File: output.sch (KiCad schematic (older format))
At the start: 14 parts

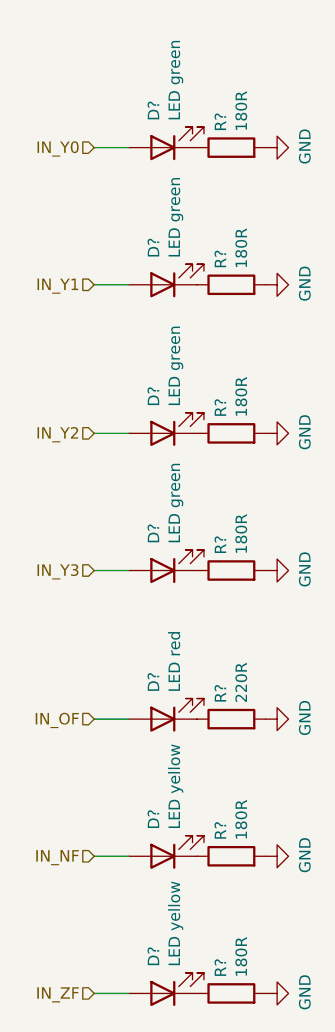
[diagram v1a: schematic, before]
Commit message: Annotate components in input and output
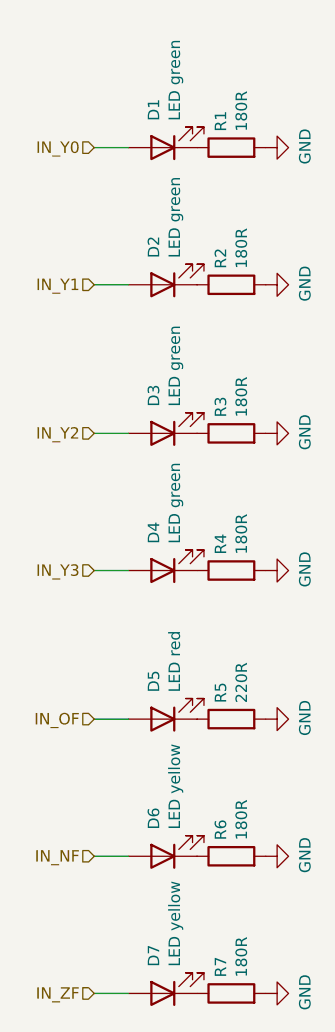
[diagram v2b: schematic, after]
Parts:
- gave numbers to parts that had none: 14
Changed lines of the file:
@@
 P 2050 1600
 AR Path="/604E77BF" Ref="D?"  Part="1"
-AR Path="/60318070/604E77BF" Ref="D?"  Part="1"
-F 0 "D?" V 2089 1483 50  0000 R CNN
+AR Path="/60318070/604E77BF" Ref="D2"  Part="1"
+F 0 "D2" V 2089 1483 50  0000 R CNN
 F 1 "LED green" V 1998 1483 50  0000 R CNN
 F 2 "LEDs:LED_0603" H 2050 1600 50  0001 C CNN
@@
 P 2350 1600
 AR Path="/604E77C6" Ref="R?"  Part="1"
-AR Path="/60318070/604E77C6" Ref="R?"  Part="1"
-F 0 "R?" H 2420 1646 50  0000 L CNN
+AR Path="/60318070/604E77C6" Ref="R2"  Part="1"
+F 0 "R2" H 2420 1646 50  0000 L CNN
 F 1 "180R" H 2420 1555 50  0000 L CNN
 F 2 "Resistors_SMD:R_0603" V 2280 1600 50  0001 C CNN
@@
 P 2050 2250
 AR Path="/604E84F3" Ref="D?"  Part="1"
-AR Path="/60318070/604E84F3" Ref="D?"  Part="1"
-F 0 "D?" V 2089 2133 50  0000 R CNN
+AR Path="/60318070/604E84F3" Ref="D3"  Part="1"
+F 0 "D3" V 2089 2133 50  0000 R CNN
 F 1 "LED green" V 1998 2133 50  0000 R CNN
 F 2 "LEDs:LED_0603" H 2050 2250 50  0001 C CNN
@@
 P 2350 2250
 AR Path="/604E84FA" Ref="R?"  Part="1"
-AR Path="/60318070/604E84FA" Ref="R?"  Part="1"
-F 0 "R?" H 2420 2296 50  0000 L CNN
+AR Path="/60318070/604E84FA" Ref="R3"  Part="1"
+F 0 "R3" H 2420 2296 50  0000 L CNN
 F 1 "180R" H 2420 2205 50  0000 L CNN
 F 2 "Resistors_SMD:R_0603" V 2280 2250 50  0001 C CNN
@@
 P 2050 2850
 AR Path="/604E912A" Ref="D?"  Part="1"
-AR Path="/60318070/604E912A" Ref="D?"  Part="1"
-F 0 "D?" V 2089 2733 50  0000 R CNN
+AR Path="/60318070/604E912A" Ref="D4"  Part="1"
+F 0 "D4" V 2089 2733 50  0000 R CNN
 F 1 "LED green" V 1998 2733 50  0000 R CNN
 F 2 "LEDs:LED_0603" H 2050 2850 50  0001 C CNN
@@
 P 2350 2850
 AR Path="/604E9131" Ref="R?"  Part="1"
-AR Path="/60318070/604E9131" Ref="R?"  Part="1"
-F 0 "R?" H 2420 2896 50  0000 L CNN
+AR Path="/60318070/604E9131" Ref="R4"  Part="1"
+F 0 "R4" H 2420 2896 50  0000 L CNN
 F 1 "180R" H 2420 2805 50  0000 L CNN
 F 2 "Resistors_SMD:R_0603" V 2280 2850 50  0001 C CNN
@@
 P 2350 3500
 AR Path="/60506BF5" Ref="R?"  Part="1"
-AR Path="/60318070/60506BF5" Ref="R?"  Part="1"
-F 0 "R?" H 2420 3546 50  0000 L CNN
+AR Path="/60318070/60506BF5" Ref="R5"  Part="1"
+F 0 "R5" H 2420 3546 50  0000 L CNN
 F 1 "220R" H 2420 3455 50  0000 L CNN
 F 2 "Resistors_SMD:R_0603" V 2280 3500 50  0001 C CNN
@@
 P 2050 3500
 AR Path="/60506BFC" Ref="D?"  Part="1"
-AR Path="/60318070/60506BFC" Ref="D?"  Part="1"
-F 0 "D?" V 2089 3383 50  0000 R CNN
+AR Path="/60318070/60506BFC" Ref="D5"  Part="1"
+F 0 "D5" V 2089 3383 50  0000 R CNN
 F 1 "LED red" V 1998 3383 50  0000 R CNN
 F 2 "LEDs:LED_0603" H 2050 3500 50  0001 C CNN
@@
 	1750 3500 1900 3500
 $Comp
-L Device:LED D?
+L Device:LED D6
 U 1 1 6052228B
 P 2050 4100
-F 0 "D?" V 2089 3983 50  0000 R CNN
+F 0 "D6" V 2089 3983 50  0000 R CNN
 F 1 "LED yellow" V 1998 3983 50  0000 R CNN
 F 2 "LEDs:LED_0603" H 2050 4100 50  0001 C CNN
@@
 $EndComp
 $Comp
-L Device:R R?
+L Device:R R6
 U 1 1 60522292
 P 2350 4100
-F 0 "R?" H 2420 4146 50  0000 L CNN
+F 0 "R6" H 2420 4146 50  0000 L CNN
 F 1 "180R" H 2420 4055 50  0000 L CNN
 F 2 "Resistors_SMD:R_0603" V 2280 4100 50  0001 C CNN
@@
 $EndComp
 $Comp
-L Device:LED D?
+L Device:LED D7
 U 1 1 60522C47
 P 2050 4700
-F 0 "D?" V 2089 4583 50  0000 R CNN
+F 0 "D7" V 2089 4583 50  0000 R CNN
 F 1 "LED yellow" V 1998 4583 50  0000 R CNN
 F 2 "LEDs:LED_0603" H 2050 4700 50  0001 C CNN
@@
 $EndComp
 $Comp
-L Device:R R?
+L Device:R R7
 U 1 1 60522C4E
 P 2350 4700
-F 0 "R?" H 2420 4746 50  0000 L CNN
+F 0 "R7" H 2420 4746 50  0000 L CNN
 F 1 "180R" H 2420 4655 50  0000 L CNN
 F 2 "Resistors_SMD:R_0603" V 2280 4700 50  0001 C CNN
@@
 P 2350 1000
 AR Path="/604E723F" Ref="R?"  Part="1"
-AR Path="/60318070/604E723F" Ref="R?"  Part="1"
-F 0 "R?" H 2420 1046 50  0000 L CNN
+AR Path="/60318070/604E723F" Ref="R1"  Part="1"
+F 0 "R1" H 2420 1046 50  0000 L CNN
 F 1 "180R" H 2420 955 50  0000 L CNN
 F 2 "Resistors_SMD:R_0603" V 2280 1000 50  0001 C CNN
@@
 P 2050 1000
 AR Path="/604E7238" Ref="D?"  Part="1"
-AR Path="/60318070/604E7238" Ref="D?"  Part="1"
-F 0 "D?" V 2089 883 50  0000 R CNN
+AR Path="/60318070/604E7238" Ref="D1"  Part="1"
+F 0 "D1" V 2089 883 50  0000 R CNN
 F 1 "LED green" V 1998 883 50  0000 R CNN
 F 2 "LEDs:LED_0603" H 2050 1000 50  0001 C CNN

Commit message: fixed some footprints
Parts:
- D1: footprint LEDs:LED_0603 -> LED_SMD:LED_0603_1608Metric
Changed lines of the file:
@@
 F 0 "D1" V 2089 883 50  0000 R CNN
 F 1 "LED green" V 1998 883 50  0000 R CNN
-F 2 "LEDs:LED_0603" H 2050 1000 50  0001 C CNN
+F 2 "LED_SMD:LED_0603_1608Metric" H 2050 1000 50  0001 C CNN
 F 3 "https://datasheet.lcsc.com/szlcsc/1811101510_Everlight-Elec-19-217-GHC-YR1S2-3T_C72043.pdf" H 2050 1000 50  0001 C CNN
 F 4 "C72043" V 2050 1000 50  0001 C CNN "LCSC"

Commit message: Change R, C and LED footprints
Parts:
- D2, D3, D4, D5, D6, D7: footprint LEDs:LED_0603 -> LED_SMD:LED_0603_1608Metric
- R1, R2, R3, R4, R5, R6, R7: footprint Resistors_SMD:R_0603 -> Resistor_SMD:R_0603_1608Metric
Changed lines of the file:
@@
 F 0 "D2" V 2089 1483 50  0000 R CNN
 F 1 "LED green" V 1998 1483 50  0000 R CNN
-F 2 "LEDs:LED_0603" H 2050 1600 50  0001 C CNN
+F 2 "LED_SMD:LED_0603_1608Metric" H 2050 1600 50  0001 C CNN
 F 3 "https://datasheet.lcsc.com/szlcsc/1811101510_Everlight-Elec-19-217-GHC-YR1S2-3T_C72043.pdf" H 2050 1600 50  0001 C CNN
 F 4 "C72043" V 2050 1600 50  0001 C CNN "LCSC"
@@
 F 0 "R2" H 2420 1646 50  0000 L CNN
 F 1 "180R" H 2420 1555 50  0000 L CNN
-F 2 "Resistors_SMD:R_0603" V 2280 1600 50  0001 C CNN
+F 2 "Resistor_SMD:R_0603_1608Metric" V 2280 1600 50  0001 C CNN
 F 3 "https://datasheet.lcsc.com/szlcsc/Uniroyal-Elec-0603WAF1800T5E_C22828.pdf" H 2350 1600 50  0001 C CNN
 F 4 "C22828" H 2350 1600 50  0001 C CNN "LCSC"
@@
 F 0 "D3" V 2089 2133 50  0000 R CNN
 F 1 "LED green" V 1998 2133 50  0000 R CNN
-F 2 "LEDs:LED_0603" H 2050 2250 50  0001 C CNN
+F 2 "LED_SMD:LED_0603_1608Metric" H 2050 2250 50  0001 C CNN
 F 3 "https://datasheet.lcsc.com/szlcsc/1811101510_Everlight-Elec-19-217-GHC-YR1S2-3T_C72043.pdf" H 2050 2250 50  0001 C CNN
 F 4 "C72043" V 2050 2250 50  0001 C CNN "LCSC"
@@
 F 0 "R3" H 2420 2296 50  0000 L CNN
 F 1 "180R" H 2420 2205 50  0000 L CNN
-F 2 "Resistors_SMD:R_0603" V 2280 2250 50  0001 C CNN
+F 2 "Resistor_SMD:R_0603_1608Metric" V 2280 2250 50  0001 C CNN
 F 3 "https://datasheet.lcsc.com/szlcsc/Uniroyal-Elec-0603WAF1800T5E_C22828.pdf" H 2350 2250 50  0001 C CNN
 F 4 "C22828" H 2350 2250 50  0001 C CNN "LCSC"
@@
 F 0 "D4" V 2089 2733 50  0000 R CNN
 F 1 "LED green" V 1998 2733 50  0000 R CNN
-F 2 "LEDs:LED_0603" H 2050 2850 50  0001 C CNN
+F 2 "LED_SMD:LED_0603_1608Metric" H 2050 2850 50  0001 C CNN
 F 3 "https://datasheet.lcsc.com/szlcsc/1811101510_Everlight-Elec-19-217-GHC-YR1S2-3T_C72043.pdf" H 2050 2850 50  0001 C CNN
 F 4 "C72043" V 2050 2850 50  0001 C CNN "LCSC"
@@
 F 0 "R4" H 2420 2896 50  0000 L CNN
 F 1 "180R" H 2420 2805 50  0000 L CNN
-F 2 "Resistors_SMD:R_0603" V 2280 2850 50  0001 C CNN
+F 2 "Resistor_SMD:R_0603_1608Metric" V 2280 2850 50  0001 C CNN
 F 3 "https://datasheet.lcsc.com/szlcsc/Uniroyal-Elec-0603WAF1800T5E_C22828.pdf" H 2350 2850 50  0001 C CNN
 F 4 "C22828" H 2350 2850 50  0001 C CNN "LCSC"
@@
 F 0 "R5" H 2420 3546 50  0000 L CNN
 F 1 "220R" H 2420 3455 50  0000 L CNN
-F 2 "Resistors_SMD:R_0603" V 2280 3500 50  0001 C CNN
+F 2 "Resistor_SMD:R_0603_1608Metric" V 2280 3500 50  0001 C CNN
 F 3 "https://datasheet.lcsc.com/szlcsc/Uniroyal-Elec-0603WAF2200T5E_C22962.pdf" H 2350 3500 50  0001 C CNN
 F 4 "C22962" H 2350 3500 50  0001 C CNN "LCSC"
@@
 F 0 "D5" V 2089 3383 50  0000 R CNN
 F 1 "LED red" V 1998 3383 50  0000 R CNN
-F 2 "LEDs:LED_0603" H 2050 3500 50  0001 C CNN
+F 2 "LED_SMD:LED_0603_1608Metric" H 2050 3500 50  0001 C CNN
 F 3 "https://datasheet.lcsc.com/szlcsc/Hubei-KENTO-Elec-KT-0603R_C2286.pdf" H 2050 3500 50  0001 C CNN
 F 4 "C2286" V 2050 3500 50  0001 C CNN "LCSC"
@@
 F 0 "D6" V 2089 3983 50  0000 R CNN
 F 1 "LED yellow" V 1998 3983 50  0000 R CNN
-F 2 "LEDs:LED_0603" H 2050 4100 50  0001 C CNN
+F 2 "LED_SMD:LED_0603_1608Metric" H 2050 4100 50  0001 C CNN
 F 3 "https://datasheet.lcsc.com/szlcsc/1810101813_Everlight-Elec-19-213-Y2C-CQ2R2L-3T-CY_C72038.pdf" H 2050 4100 50  0001 C CNN
 F 4 "C72038" V 2050 4100 50  0001 C CNN "LCSC"
@@
 F 0 "R6" H 2420 4146 50  0000 L CNN
 F 1 "180R" H 2420 4055 50  0000 L CNN
-F 2 "Resistors_SMD:R_0603" V 2280 4100 50  0001 C CNN
+F 2 "Resistor_SMD:R_0603_1608Metric" V 2280 4100 50  0001 C CNN
 F 3 "https://datasheet.lcsc.com/szlcsc/Uniroyal-Elec-0603WAF1800T5E_C22828.pdf" H 2350 4100 50  0001 C CNN
 F 4 "C22828" H 2350 4100 50  0001 C CNN "LCSC"
@@
 F 0 "D7" V 2089 4583 50  0000 R CNN
 F 1 "LED yellow" V 1998 4583 50  0000 R CNN
-F 2 "LEDs:LED_0603" H 2050 4700 50  0001 C CNN
+F 2 "LED_SMD:LED_0603_1608Metric" H 2050 4700 50  0001 C CNN
 F 3 "https://datasheet.lcsc.com/szlcsc/1810101813_Everlight-Elec-19-213-Y2C-CQ2R2L-3T-CY_C72038.pdf" H 2050 4700 50  0001 C CNN
 F 4 "C72038" V 2050 4700 50  0001 C CNN "LCSC"
@@
 F 0 "R7" H 2420 4746 50  0000 L CNN
 F 1 "180R" H 2420 4655 50  0000 L CNN
-F 2 "Resistors_SMD:R_0603" V 2280 4700 50  0001 C CNN
+F 2 "Resistor_SMD:R_0603_1608Metric" V 2280 4700 50  0001 C CNN
 F 3 "https://datasheet.lcsc.com/szlcsc/Uniroyal-Elec-0603WAF1800T5E_C22828.pdf" H 2350 4700 50  0001 C CNN
 F 4 "C22828" H 2350 4700 50  0001 C CNN "LCSC"
@@
 F 0 "R1" H 2420 1046 50  0000 L CNN
 F 1 "180R" H 2420 955 50  0000 L CNN
-F 2 "Resistors_SMD:R_0603" V 2280 1000 50  0001 C CNN
+F 2 "Resistor_SMD:R_0603_1608Metric" V 2280 1000 50  0001 C CNN
 F 3 "https://datasheet.lcsc.com/szlcsc/Uniroyal-Elec-0603WAF1800T5E_C22828.pdf" H 2350 1000 50  0001 C CNN
 F 4 "C22828" H 2350 1000 50  0001 C CNN "LCSC"
